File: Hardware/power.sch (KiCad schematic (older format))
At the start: 9 parts, among them J1 Screw_Terminal_01x02, U4 LM317_TO-252

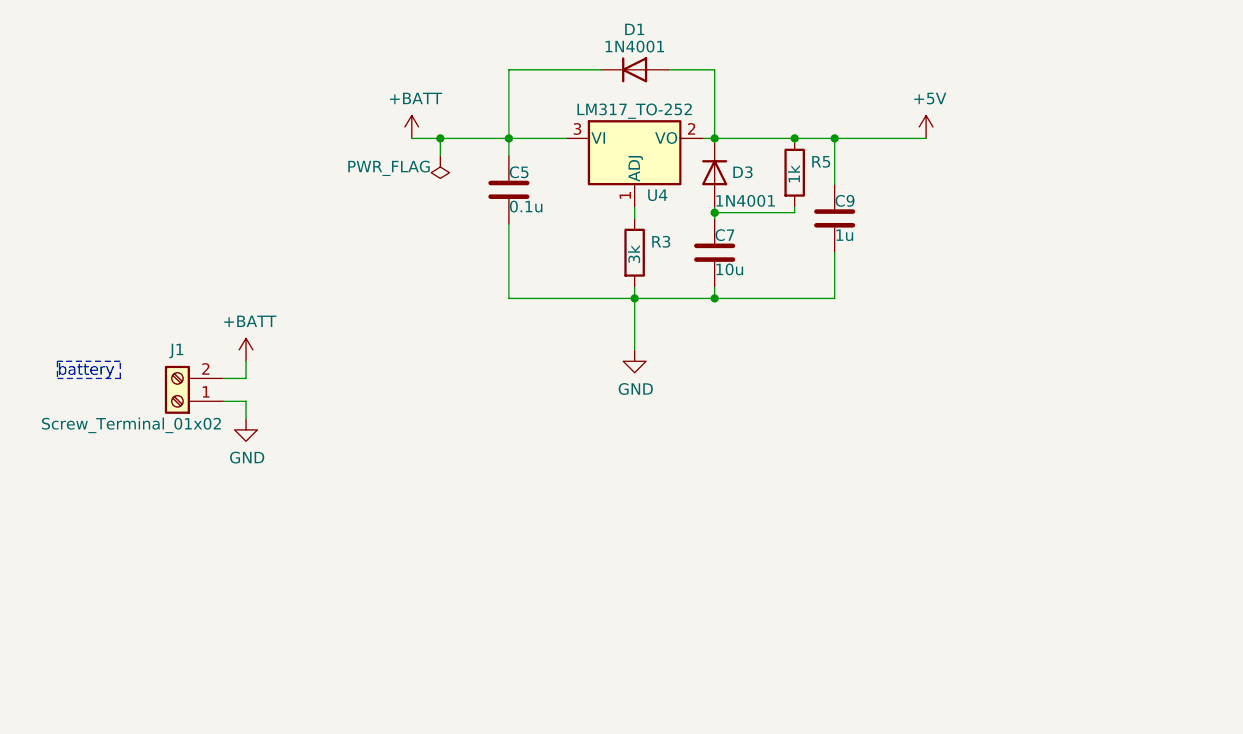
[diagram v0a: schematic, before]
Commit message: Update schematic, component placement
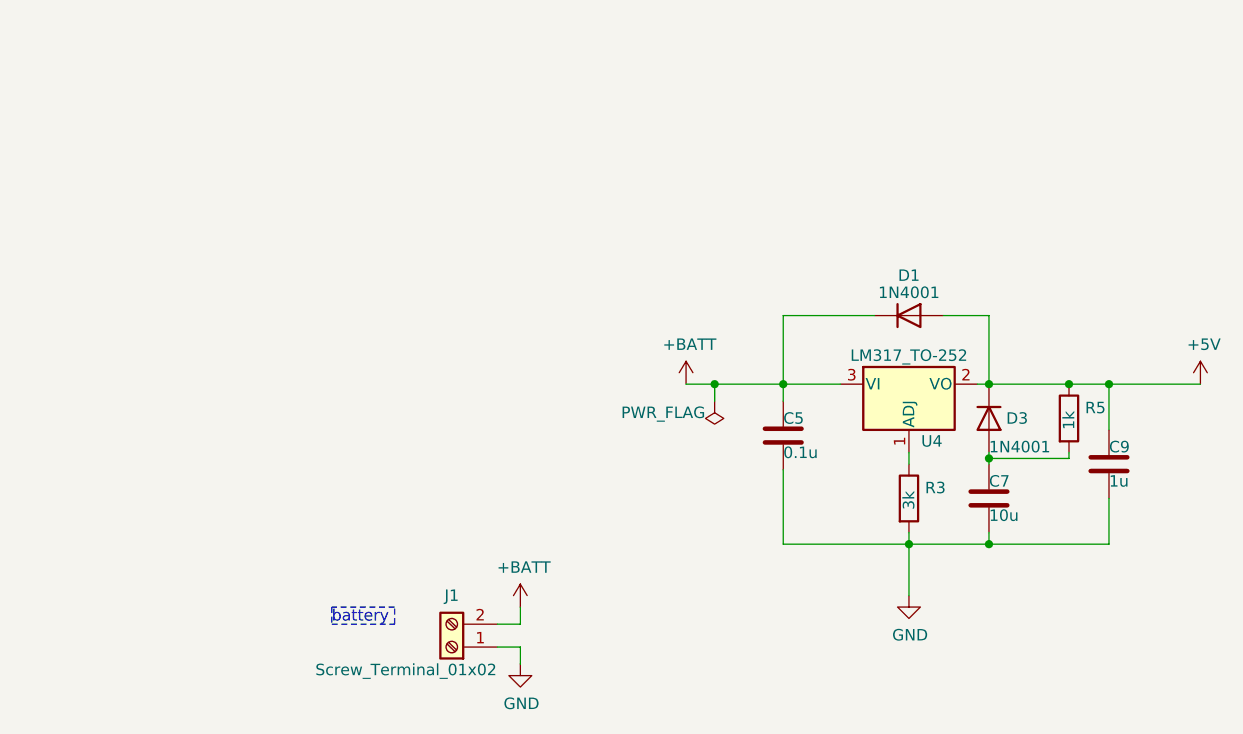
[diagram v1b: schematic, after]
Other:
- moved on the sheet: C5, C7, C9, D1, D3, J1, R3, R5, U4

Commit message: Change regulator diode footprint, update routing
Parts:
- D1, D3: footprint Diode_SMD:D_SOD-123 -> Diode_SMD:D_SOD-123F; MANUFACTURER (none) -> Shandong Jingdao Microelectronics; Manufacturer_Part_Number (none) -> 1N4001W
- U4: MANUFACTURER (none) -> UTC(Unisonic Tech); Manufacturer_Part_Number (none) -> LM317AG-TN3-R
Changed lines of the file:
@@
 F 2 "Package_TO_SOT_SMD:TO-252-2" H 6025 3550 50  0001 C CIN
 F 3 "http://www.ti.com/lit/ds/snvs774n/snvs774n.pdf" H 6025 3300 50  0001 C CNN
+F 4 "UTC(Unisonic Tech)" H 6025 3300 50  0001 C CNN "MANUFACTURER"
+F 5 "LM317AG-TN3-R" H 6025 3300 50  0001 C CNN "Manufacturer_Part_Number"
 	1    6025 3300
 	1    0    0    -1
@@
 F 0 "D1" H 6025 3175 50  0000 C CNN
 F 1 "1N4001" H 6025 3100 50  0000 C CNN
-F 2 "Diode_SMD:D_SOD-123" H 6025 3000 50  0001 C CNN
+F 2 "Diode_SMD:D_SOD-123F" H 6025 3000 50  0001 C CNN
 F 3 "~" H 6025 3000 50  0001 C CNN
+F 4 "Shandong Jingdao Microelectronics" H 6025 3000 50  0001 C CNN "MANUFACTURER"
+F 5 "1N4001W" H 6025 3000 50  0001 C CNN "Manufacturer_Part_Number"
 	1    6025 3000
 	1    0    0    -1
@@
 F 0 "D3" V 6375 3525 50  0000 L CNN
 F 1 "1N4001" V 6500 3450 50  0000 L CNN
-F 2 "Diode_SMD:D_SOD-123" H 6375 3450 50  0001 C CNN
+F 2 "Diode_SMD:D_SOD-123F" H 6375 3450 50  0001 C CNN
 F 3 "~" H 6375 3450 50  0001 C CNN
+F 4 "Shandong Jingdao Microelectronics" H 6375 3450 50  0001 C CNN "MANUFACTURER"
+F 5 "1N4001W" H 6375 3450 50  0001 C CNN "Manufacturer_Part_Number"
 	1    6375 3450
 	0    1    1    0
